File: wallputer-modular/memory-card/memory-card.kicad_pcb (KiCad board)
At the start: 2 copper layers, 99.7 x 99.7 mm, 1 part

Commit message: begin wiring memory card
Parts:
- added C1: 100nF, Capacitor_THT:C_Disc_D5.0mm_W2.5mm_P5.00mm, F.Cu at (108.6, 82.5)
- added C2: 100nF, Capacitor_THT:C_Disc_D5.0mm_W2.5mm_P5.00mm, F.Cu at (131.4, 87.6)
- added C3: 100nF, Capacitor_THT:C_Disc_D5.0mm_W2.5mm_P5.00mm, F.Cu at (82.5, 82.5)
- added R1: 10k, Resistor_THT:R_Axial_DIN0204_L3.6mm_D1.6mm_P2.54mm_Vertical, F.Cu at (111.8, 88.9)
- added U1: HM62256BLP, Package_DIP:DIP-28_W7.62mm_Socket, F.Cu at (123.8, 91.4)
- added U2: 74HC00, Package_DIP:DIP-14_W7.62mm_Socket, F.Cu at (74.9, 86.4)
- added U3: SST39SF010, Package_DIP:DIP-32_W15.24mm_Socket, F.Cu at (93.3, 86.4)
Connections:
- J1 pad 10: unconnected-(J1-A5-Pad10) -> /A5
- J1 pad 11: unconnected-(J1-A6-Pad11) -> /A6
- J1 pad 12: unconnected-(J1-A7-Pad12) -> /A7
- J1 pad 13: unconnected-(J1-A8-Pad13) -> /A8
- J1 pad 14: unconnected-(J1-A9-Pad14) -> /A9
- J1 pad 15: unconnected-(J1-A10-Pad15) -> /A10
- J1 pad 16: unconnected-(J1-A11-Pad16) -> /A11
- J1 pad 17: unconnected-(J1-A12-Pad17) -> /A12
- J1 pad 18: unconnected-(J1-A13-Pad18) -> /A13
- J1 pad 19: unconnected-(J1-A14-Pad19) -> /A14
- J1 pad 20: unconnected-(J1-A15-Pad20) -> /A15
- J1 pad 21: unconnected-(J1-D0-Pad21) -> /D0
- J1 pad 22: unconnected-(J1-D1-Pad22) -> /D1
- J1 pad 23: unconnected-(J1-D2-Pad23) -> /D2
- J1 pad 24: unconnected-(J1-D3-Pad24) -> /D3
- J1 pad 25: unconnected-(J1-D4-Pad25) -> /D4
- J1 pad 26: unconnected-(J1-D5-Pad26) -> /D5
- J1 pad 27: unconnected-(J1-D6-Pad27) -> /D6
- J1 pad 28: unconnected-(J1-D7-Pad28) -> /D7
- J1 pad 29: unconnected-(J1-RW/-Pad29) -> RW/
- J1 pad 30: unconnected-(J1-NC-Pad30) -> ROM_PGM/
- J1 pad 35: unconnected-(J1-RAM/-Pad35) -> RAM/
- J1 pad 36: unconnected-(J1-ROM/-Pad36) -> ROM/
- J1 pad 38: unconnected-(J1-ACC/-Pad38) -> ACC/
- J1 pad 39: unconnected-(J1-CLK-Pad39) -> CLK
- J1 pad 5: unconnected-(J1-A0-Pad5) -> /A0
- J1 pad 6: unconnected-(J1-A1-Pad6) -> /A1
- J1 pad 7: unconnected-(J1-A2-Pad7) -> /A2
- J1 pad 8: unconnected-(J1-A3-Pad8) -> /A3
- J1 pad 9: unconnected-(J1-A4-Pad9) -> /A4
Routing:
- net +5V: track 2.54 -> 79.5 mm
- net ROM_PGM/: track 0.00 -> 3.18 mm

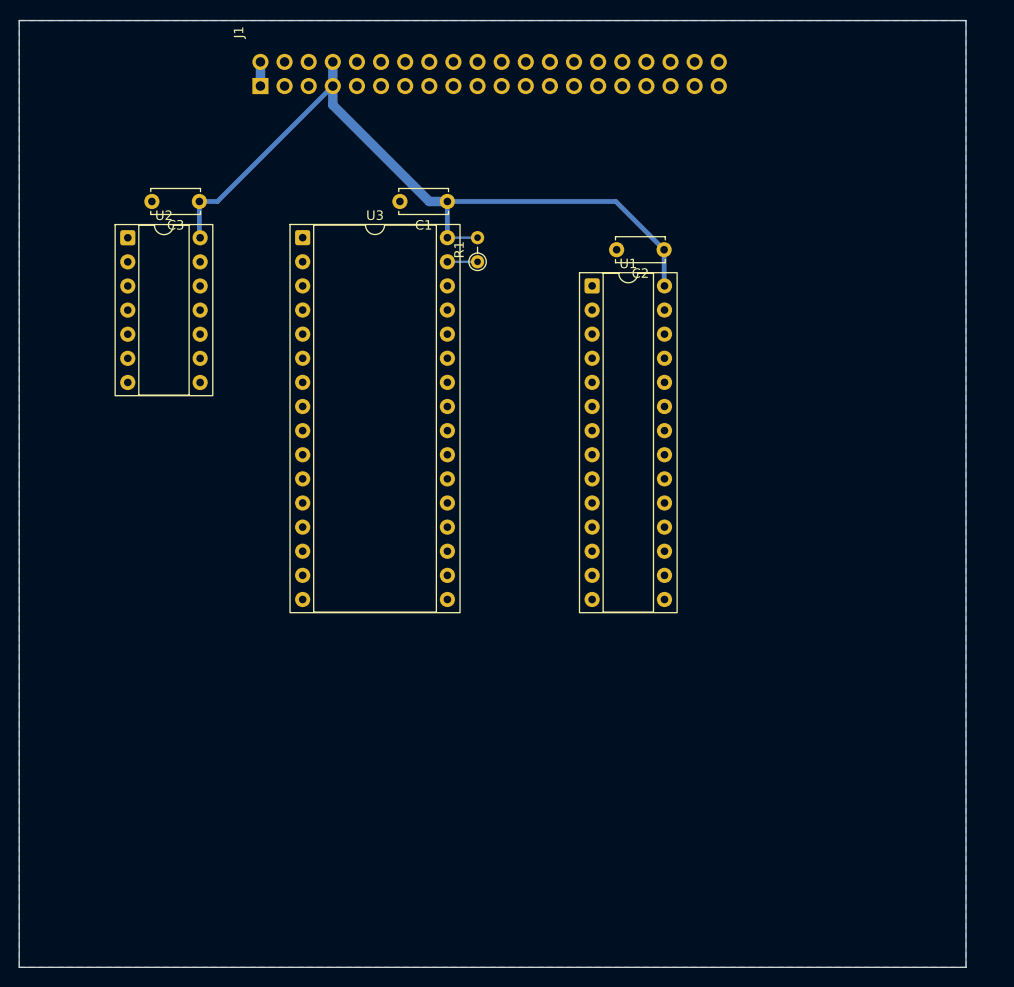
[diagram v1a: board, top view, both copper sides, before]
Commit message: wire up memory card
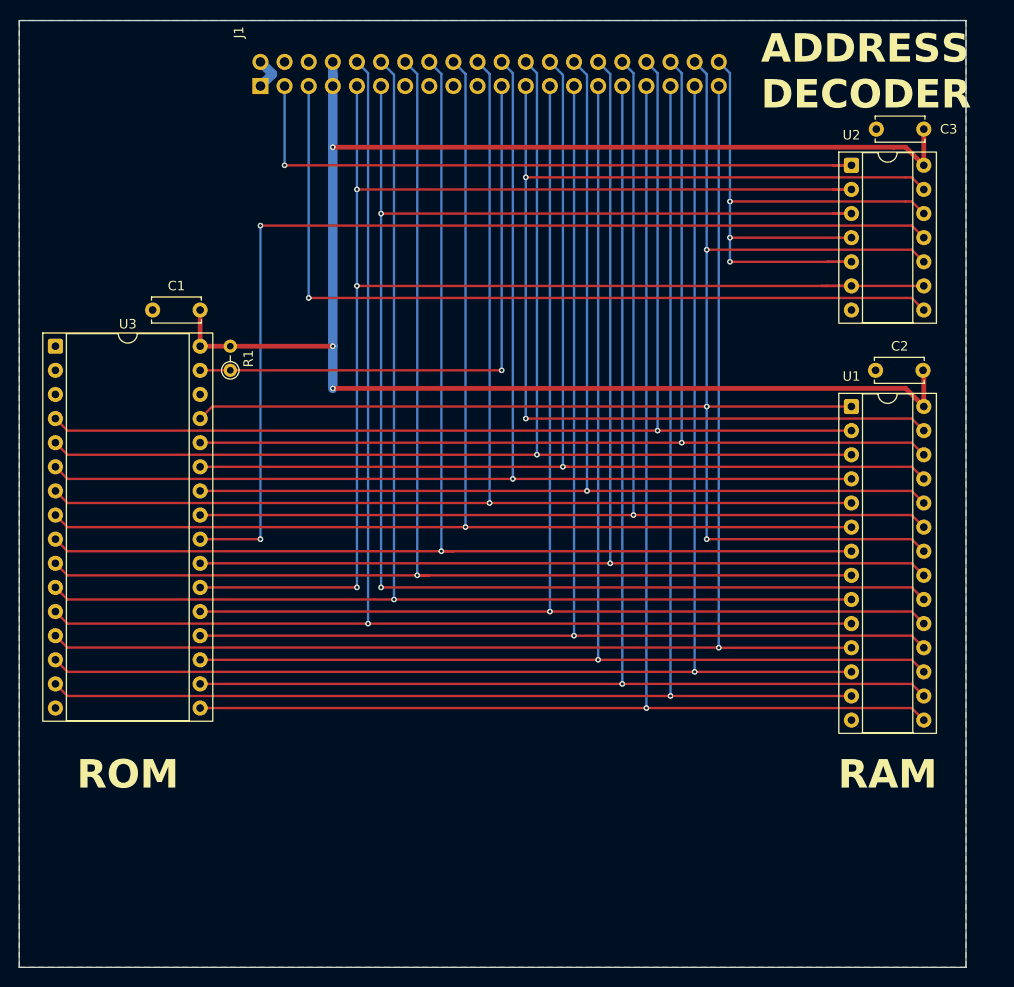
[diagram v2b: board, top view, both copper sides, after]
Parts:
- moved C3 76.7 mm to (158.8, 74.9)
- moved U2 76.6 mm to (151.1, 78.7)
- moved U1 30.1 mm to (151.1, 104.1)
- moved C2 30.1 mm to (158.7, 100.3)
- moved R1 28.4 mm to (85.7, 100.3)
- moved C1 28.4 mm to (82.5, 94.0)
- moved U3 28.4 mm to (67.3, 97.8)
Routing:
- net ROM/: track 0.00 -> 184.9 mm, vias 0 -> 3
- net /A14: track 0.00 -> 166.7 mm, vias 0 -> 3
- net RAM/: track 0.00 -> 161.3 mm, vias 0 -> 2
- net /D2: track 0.00 -> 148.6 mm, vias 0 -> 1
- net /D1: track 0.00 -> 146.0 mm, vias 0 -> 1
- net /A0: track 0.00 -> 144.0 mm, vias 0 -> 1
- net /D0: track 0.00 -> 143.5 mm, vias 0 -> 1
- net /D3: track 0.00 -> 142.2 mm, vias 0 -> 1
- net /A1: track 0.00 -> 141.5 mm, vias 0 -> 1
- net /A2: track 0.00 -> 140.2 mm, vias 0 -> 1
- net /D4: track 0.00 -> 139.7 mm, vias 0 -> 1
- net /A3: track 0.00 -> 137.7 mm, vias 0 -> 1
- net /D5: track 0.00 -> 137.1 mm, vias 0 -> 1
- net /D6: track 0.00 -> 134.6 mm, vias 0 -> 1
- net /A4: track 0.00 -> 133.9 mm, vias 0 -> 1
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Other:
- board text added: "ADDRESS DECODER"
- board text added: "RAM"
- board text added: "ROM"
